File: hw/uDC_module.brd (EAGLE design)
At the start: 25 x 45 mm, 38 parts, among them J1 GROVE-4P-2.0-3470130P1, J2 GROVE-4P-2.0-3470130P1, U5 LD3985XX, X1 22-23-2021, X2 22-23-2021, X3 53047-06, X4 53047-06

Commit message: added blinking led firmware
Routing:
- net GND: vias 53 -> 55
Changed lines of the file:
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@@
 <contactref element="X3" pad="4"/>
 <contactref element="X3" pad="6"/>
+<via x="14.3" y="9.7" extent="1-16" drill="0.3"/>
+<via x="15.1" y="9.7" extent="1-16" drill="0.3"/>
 </signal>
 <signal name="VIN">

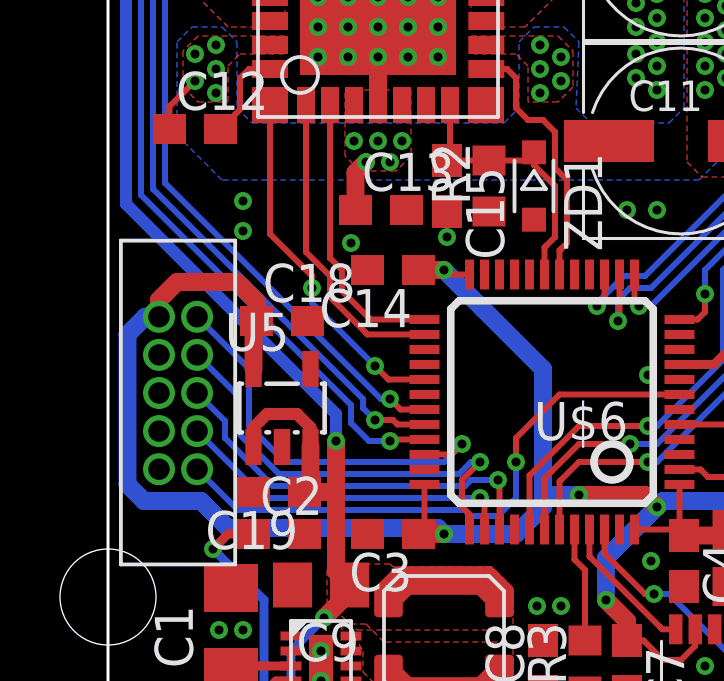
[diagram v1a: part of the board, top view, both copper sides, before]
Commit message: moved IN2 to TIM1 ch2
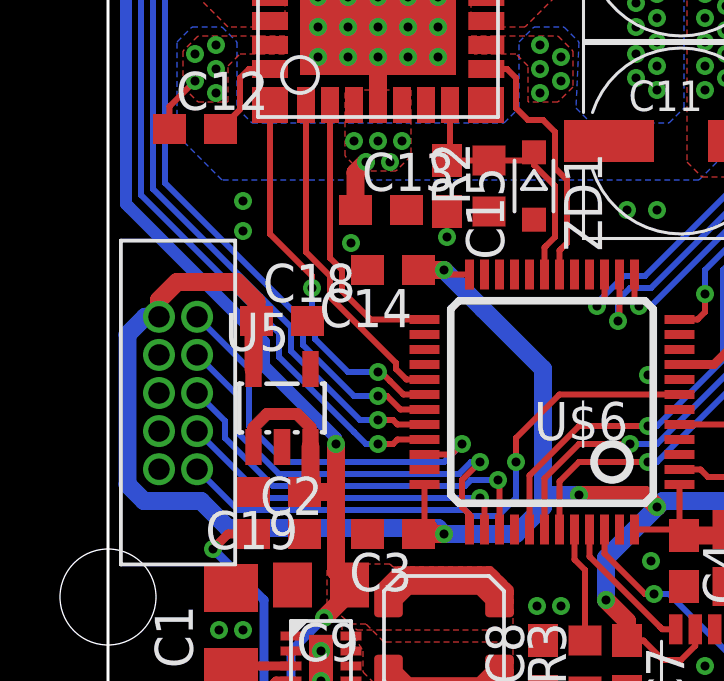
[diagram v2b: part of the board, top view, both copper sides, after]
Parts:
- C15: value 100n -> 470n
- R2: value 10k -> 220
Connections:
- net ANALOG renamed ENC_ANALOG
- net IN1: now also U$6.29; no longer U$6.26
- net IN2: now also U$6.30; no longer U$6.29
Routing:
- net IN2: track 12.0 -> 12.8 mm
- net IN1: track 10.4 -> 11.1 mm

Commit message: small fixes for production
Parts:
- removed R3: 10k, rcl:R0603
- added RN1: 4k7, dp_devices:RN8P-4R-CRA06S
- added SJ1: SOLDERJUMPERTRACE, SparkFun:SJ_2S-TRACE
- moved R1 9.27 mm to (15.9, 7.70), turned to 90 degrees
- moved C6 4.00 mm to (22.7, 14.0)
- moved C17 1.40 mm to (22.7, 18.0)
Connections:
- removed net BOOT0: R3.2, U$6.44
- new net N$5: RN1.6, RN1.7, RN1.8, SJ1.1
- net +3V3: now also SJ1.2
- net ENC_A: now also RN1.2
- net ENC_B: now also RN1.1
- net ENC_I: now also RN1.3
- net GND: now also U$6.44; no longer R3.1
- net LED1: now also U$6.6; no longer U$6.2
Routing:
- net N$4: track 18.0 -> 4.61 mm, vias 2 -> 0
- net LED1: track 2.90 -> 11.1 mm, vias 0 -> 2
- net N$5: track 0.00 -> 4.53 mm, vias 0 -> 1
- net BOOT0: track 3.84 -> 0.00 mm
- net +3V3: track 83.3 -> 81.2 mm, vias 8 -> 7
- net ENC_B: track 45.7 -> 46.9 mm, vias 1 -> 2
- net ENC_I: track 44.1 -> 45.2 mm, vias 1 -> 2
- net ENC_A: track 43.7 -> 44.8 mm, vias 1 -> 2
- net GND: vias 55 -> 53
